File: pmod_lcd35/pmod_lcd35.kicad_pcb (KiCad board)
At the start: 2 copper layers, 65 x 75 mm, 20 parts, among them J1 PMOD_0, J2 PMOD_1, U1 TPS61165

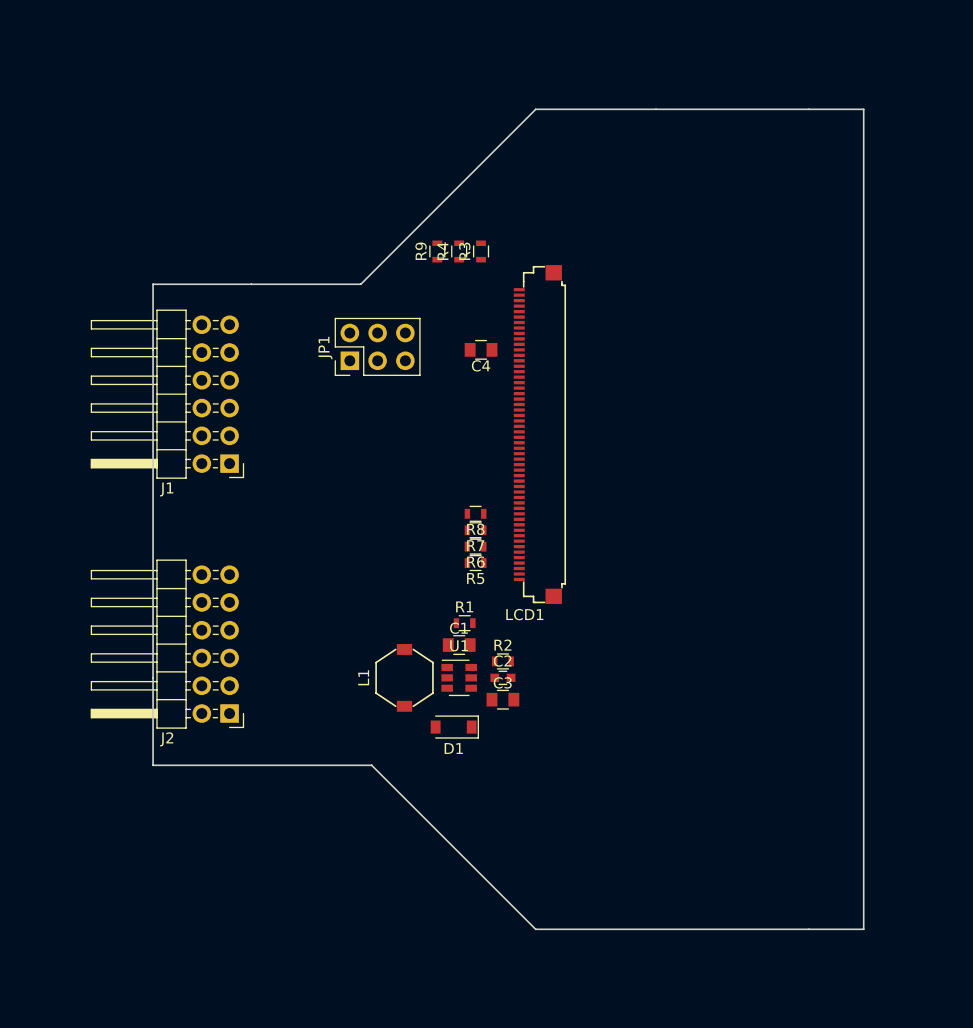
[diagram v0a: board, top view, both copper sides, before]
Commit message: LCD PMOD PCB routed
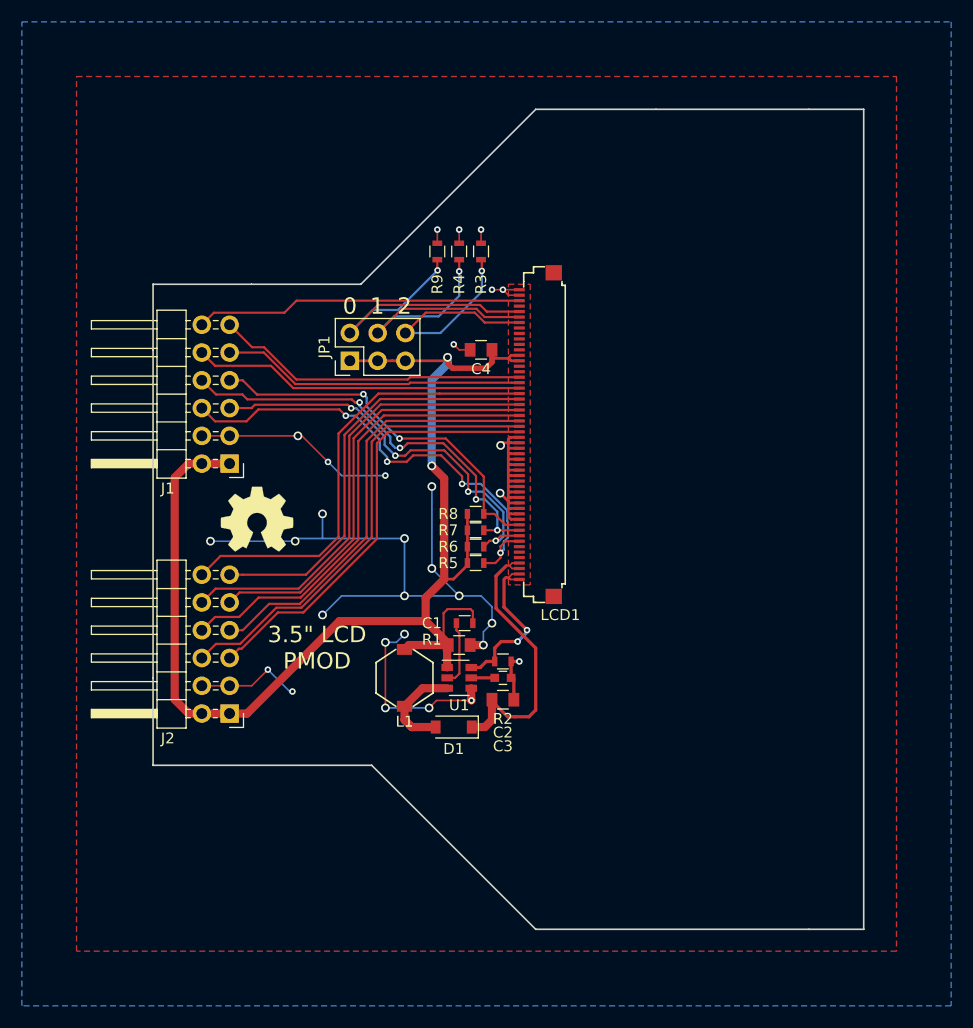
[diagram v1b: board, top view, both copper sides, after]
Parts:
- added REF***: OSHW-Symbol_6.7x6mm_SilkScreen, Symbols:OSHW-Symbol_6.7x6mm_SilkScreen, F.Cu at (116.5, 70.5)
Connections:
- LCD1 pad 28: /DX1 -> /DX0
- LCD1 pad 29: (no net) -> /DX1
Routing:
- net GND: track 0.00 -> 143.0 mm, vias 0 -> 30
- net +3V3: track 0.00 -> 121.3 mm, vias 0 -> 2
- net /~RESET: track 0.00 -> 43.3 mm, vias 0 -> 4
- net /DX1: track 0.00 -> 42.9 mm
- net /DX3: track 0.00 -> 42.5 mm
- net /DX5: track 0.00 -> 42.0 mm
- net /DX7: track 0.00 -> 41.4 mm
- net /DX0: track 0.00 -> 40.2 mm
- net /DX2: track 0.00 -> 39.6 mm
- net /DX4: track 0.00 -> 39.2 mm
- net /SPCLK: track 0.00 -> 39.1 mm, vias 0 -> 4
- net /DX6: track 0.00 -> 38.6 mm
- net /SPENA: track 0.00 -> 37.8 mm, vias 0 -> 4
- net /SPDAT: track 0.00 -> 34.5 mm, vias 0 -> 2
- net /HSYNC: track 0.00 -> 30.4 mm
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- added copper zone on B.Cu, net GND
- added copper zone on F.Cu, net GND
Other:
- net class Default: trace_width 0.25 -> 0.1524; via_dia 0.8 -> 0.6; via_drill 0.4 -> 0.3
- rule pad_to_mask_clearance: 0.2 -> 0
- rule trace_min: 0.2 -> 0.1524
- rule via_min_size: 0.4 -> 0.6
- board text added: "0"
- board text added: "1"
- board text added: "2"
- board text added: "3.5" LCD PMOD"
